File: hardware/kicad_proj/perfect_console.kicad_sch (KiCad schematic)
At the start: 71 parts, among them J1 R_Out, J10 PWR_OUT_Pins, J11 GPIO5-7, J12 USB_Out, J13 I2C, J14 ESP_UART, J15 GPIO41, J16 CH_UART, J17 CH_Flash, J18 Micro_SD_Card, J2 Jack_3.5, J3 L_Out, J4 USB, J5 TP4056_WO_Protect, J6 Bat, J7 PWR_Btn, J8 BTN_Pins, J9 PTT_Btn, Q1 NMOS, Q2 NMOS, Q3 NMOS, Q4 NMOS, Q5 NMOS, Q6 NMOS, SW1 Reset, SW2 Boot, U1 ESP32-S3-WROOM1, U2 Display, U3 PCM5102, U4 PAM8403, U5 CH32V006E8R6, U6 LoRa, U7 USBLC6-2SC6, U8 Mic, U9 DC-DC

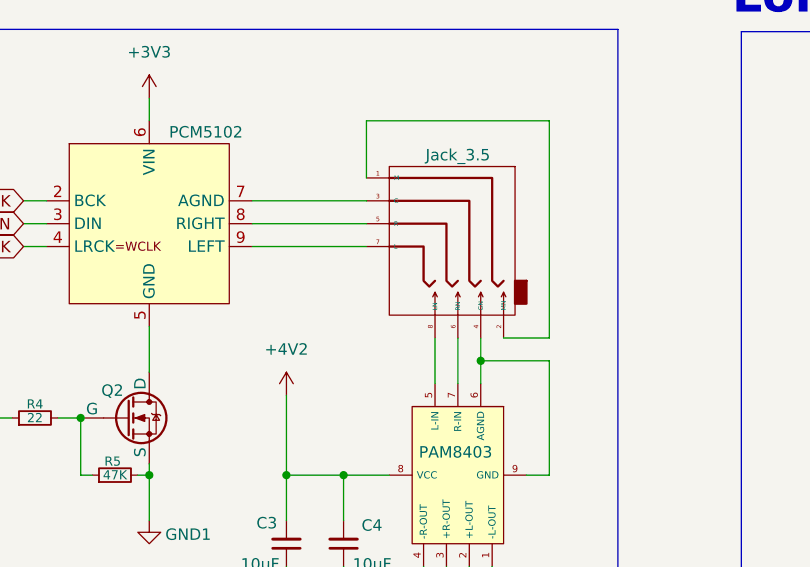
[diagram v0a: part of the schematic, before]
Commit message: Виправлено символ
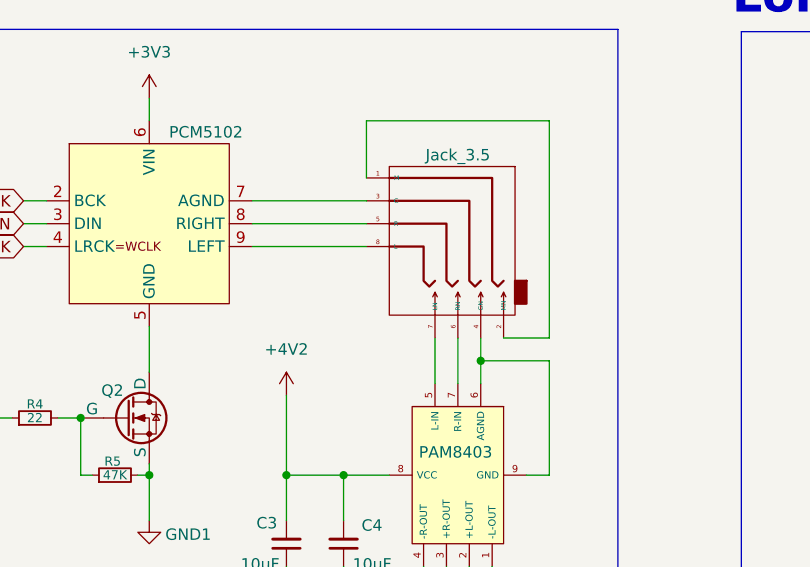
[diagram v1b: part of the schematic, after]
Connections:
- net at J2.7 (LN): now also U4.5 (L-IN); no longer U3.9 (LEFT)
- net at J2.8 (L): now also U3.9 (LEFT); no longer U4.5 (L-IN)

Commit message: Виправлено імена міток
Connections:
- net DISP_EN renamed DISP_PWR
- net LORA_EN renamed LORA_PWR
- net MIC_EN renamed MIC_PWR
- net POWER_EN renamed BOARD_PWR
- net SPK_EN renamed SPK_PWR
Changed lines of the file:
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@@
 		)
 	)
-	(global_label "DISP_EN"
+	(global_label "DISP_PWR"
 		(shape output)
 		(at 222.25 80.01 0)
@@
 		)
 		(property "Intersheetrefs" "${INTERSHEET_REFS}"
-			(at 233.0366 80.01 0)
+			(at 234.5485 80.01 0)
 			(effects
 				(font
@@
 		)
 	)
-	(global_label "SPK_EN"
+	(global_label "SPK_PWR"
 		(shape input)
 		(at 121.92 218.44 180)
@@
 		)
 		(property "Intersheetrefs" "${INTERSHEET_REFS}"
-			(at 111.7382 218.44 0)
-			(effects
-				(font
-					(size 1.27 1.27)
-				)
-				(justify right)
-				(hide yes)
-			)
-		)
-	)
-	(global_label "LORA_EN"
+			(at 110.2263 218.44 0)
+			(effects
+				(font
+					(size 1.27 1.27)
+				)
+				(justify right)
+				(hide yes)
+			)
+		)
+	)
+	(global_label "LORA_PWR"
 		(shape output)
 		(at 222.25 85.09 0)
@@
 		)
 		(property "Intersheetrefs" "${INTERSHEET_REFS}"
-			(at 233.3995 85.09 0)
+			(at 234.9114 85.09 0)
 			(effects
 				(font
@@
 		)
 	)
-	(global_label "LORA_EN"
+	(global_label "LORA_PWR"
 		(shape input)
 		(at 245.11 232.41 180)
@@
 		)
 		(property "Intersheetrefs" "${INTERSHEET_REFS}"
-			(at 233.9605 232.41 0)
+			(at 232.4486 232.41 0)
 			(effects
 				(font
@@
 		)
 	)
-	(global_label "MIC_EN"
+	(global_label "MIC_PWR"
 		(shape output)
 		(at 222.25 77.47 0)
@@
 		)
 		(property "Intersheetrefs" "${INTERSHEET_REFS}"
-			(at 232.0085 77.47 0)
+			(at 233.5204 77.47 0)
 			(effects
 				(font
@@
 		)
 	)
-	(global_label "SPK_EN"
+	(global_label "SPK_PWR"
 		(shape output)
 		(at 222.25 97.79 0)
@@
 		)
 		(property "Intersheetrefs" "${INTERSHEET_REFS}"
-			(at 232.4318 97.79 0)
+			(at 233.9437 97.79 0)
 			(effects
 				(font
@@
 		)
 	)
+	(global_label "BOARD_PWR"
+		(shape input)
+		(at 504.19 78.74 180)
+		(fields_autoplaced yes)
+		(effects
+			(font
+				(size 1.27 1.27)
+				(color 49 0 255 1)
+			)
+			(justify right)
+		)
+		(property "Intersheetrefs" "${INTERSHEET_REFS}"
+			(at 490.0167 78.74 0)
+			(effects
+				(font
+					(size 1.27 1.27)
+				)
+				(justify right)
+				(hide yes)
+			)
+		)
+	)
 	(global_label "LR_TX"
 		(shape output)
@@
 		)
 	)
-	(global_label "POWER_EN"
-		(shape input)
-		(at 504.19 78.74 180)
-		(fields_autoplaced yes)
-		(effects
-			(font
-				(size 1.27 1.27)
-				(color 255 139 0 1)
-			)
-			(justify right)
-		)
-		(property "Intersheetrefs" "${INTERSHEET_REFS}"
-			(at 491.2868 78.74 0)
-			(effects
-				(font
-					(size 1.27 1.27)
-				)
-				(justify right)
-				(hide yes)
-			)
-		)
-	)
 	(global_label "DATA -"
 		(shape bidirectional)
@@
 		)
 	)
-	(global_label "DISP_EN"
+	(global_label "DISP_PWR"
 		(shape input)
 		(at 49.53 224.79 180)
@@
 		)
 		(property "Intersheetrefs" "${INTERSHEET_REFS}"
-			(at 38.7434 224.79 0)
+			(at 37.2315 224.79 0)
 			(effects
 				(font
@@
 		)
 	)
-	(global_label "MIC_EN"
+	(global_label "MIC_PWR"
 		(shape input)
 		(at 354.33 207.01 180)
@@
 		)
 		(property "Intersheetrefs" "${INTERSHEET_REFS}"
-			(at 344.5715 207.01 0)
+			(at 343.0596 207.01 0)
 			(effects
 				(font
@@
 		)
 	)
-	(global_label "POWER_EN"
+	(global_label "BOARD_PWR"
 		(shape output)
 		(at 222.25 82.55 0)
@@
 		)
 		(property "Intersheetrefs" "${INTERSHEET_REFS}"
-			(at 235.1532 82.55 0)
-			(effects
-				(font
+			(at 236.4233 82.55 0)
+			(effects
+				(font

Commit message: Перепрацьовано схему
Карту пам'яті і дисплей рознесено на окремі шини
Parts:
- removed J11: GPIO5-7, Connector_PinHeader_2.54mm:PinHeader_1x03_P2.54mm_Vertical, symbol Connector_Generic:Conn_01x03
- added J11: GPIO_40-41, Connector_PinHeader_2.54mm:PinHeader_1x02_P2.54mm_Vertical, symbol Connector_Generic:Conn_01x02
- J15: value GPIO41 -> GPIO10
- renumbered C15 to C14, C16 to C15, U5 to U4, U4 to U5
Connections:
- net GPIO5 is gone; now on net LR_M0: U1.5 (IO5)
- net GPIO6 is gone; now on net LR_M1: U1.6 (IO6)
- net GPIO7 is gone; now on net LR_RX: U1.7 (IO7)
- net DISP_BLK: now also U1.12 (IO8); no longer U1.33 (IO40)
- net DISP_D/C: now also U1.11 (IO18); no longer U1.31 (IO38)
- net DISP_RST: now also U1.10 (IO17), U2.5 (RES); no longer U1.32 (IO39), U2.7 (CS)
- net GND1: now also J18.2 (DAT3/CD), U2.7 (CS)
- net GPIO41: now also J11.2 (Pin_2); no longer J15.1 (Pin_1)
- net LR_AUX: now also U1.9 (IO16); no longer U1.12 (IO8)
- net LR_M0: no longer U1.8 (IO15)
- net LR_M1: no longer U1.9 (IO16)
- net LR_RX: no longer U1.10 (IO17)
- net LR_TX: now also U1.8 (IO15); no longer U1.11 (IO18)
- net DISP_CS renamed SD_MOSI
- net SD_MOSI: now also J18.3 (CMD), R19.2; no longer U2.5 (RES)
- net HSPI_MISO renamed SD_MISO
- net SD_MISO: now also U1.32 (IO39); no longer U1.21 (IO13)
- removed net HSPI_MOSI: J18.3 (CMD), R19.2, U1.19 (IO11), U2.3 (SCL)
- net HSPI_SCK renamed SD_SCK
- net SD_SCK: now also U1.31 (IO38); no longer U1.20 (IO12), U2.4 (SDA)
- net SD_CS renamed GPIO10
- net GPIO10: now also J15.1 (Pin_1); no longer J18.2 (DAT3/CD)
- new net DISP_MISO: U1.21 (IO13)
- new net DISP_MOSI: U1.19 (IO11), U2.4 (SDA)
- new net DISP_SCK: U1.20 (IO12), U2.3 (SCL)
- new net GPIO40: J11.1 (Pin_1), U1.33 (IO40)
- no-connect marks 7 -> 8

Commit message: SD_CS пін перенесено на 10 пін ESP32S3
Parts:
- removed J15: GPIO10, Connector_PinHeader_2.54mm:PinHeader_1x01_P2.54mm_Vertical, symbol Connector_Generic:Conn_01x01
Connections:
- net GND1: no longer J18.2 (DAT3/CD)
- net GPIO10 renamed SD_CS
- net SD_CS: now also J18.2 (DAT3/CD)
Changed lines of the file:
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@@
 	(wire
 		(pts
-			(xy 511.81 215.9) (xy 514.35 215.9)
-		)
-		(stroke
-			(width 0)
-			(type default)
-		)
-	)
-	(wire
-		(pts
 			(xy 217.17 80.01) (xy 222.25 80.01)
 		)
@@
 		)
 	)
-	(global_label "GPIO10"
-		(shape bidirectional)
-		(at 511.81 215.9 180)
-		(fields_autoplaced yes)
-		(effects
-			(font
-				(size 1.27 1.27)
-				(color 1 34 255 1)
-			)
-			(justify right)
-		)
-		(property "Intersheetrefs" "${INTERSHEET_REFS}"
-			(at 500.8192 215.9 0)
-			(effects
-				(font
-					(size 1.27 1.27)
-				)
-				(justify right)
-				(hide yes)
-			)
-		)
-	)
 	(global_label "BACK_BTN"
 		(shape output)
@@
 		)
 	)
+	(global_label "SD_CS"
+		(shape output)
+		(at 46.99 88.9 180)
+		(fields_autoplaced yes)
+		(effects
+			(font
+				(size 1.27 1.27)
+				(color 255 0 37 1)
+			)
+			(justify right)
+		)
+		(property "Intersheetrefs" "${INTERSHEET_REFS}"
+			(at 38.0782 88.9 0)
+			(effects
+				(font
+					(size 1.27 1.27)
+				)
+				(justify right)
+				(hide yes)
+			)
+		)
+	)
 	(global_label "TX_0"
 		(shape output)
@@
 		)
 	)
-	(global_label "GPIO10"
-		(shape bidirectional)
-		(at 46.99 88.9 180)
-		(fields_autoplaced yes)
-		(effects
-			(font
-				(size 1.27 1.27)
-				(color 1 34 255 1)
-			)
-			(justify right)
-		)
-		(property "Intersheetrefs" "${INTERSHEET_REFS}"
-			(at 35.9992 88.9 0)
-			(effects
-				(font
-					(size 1.27 1.27)
-				)
-				(justify right)
-				(hide yes)
-			)
-		)
-	)
 	(global_label "SD_SCK"
 		(shape output)
@@
 		)
 	)
+	(global_label "SD_CS"
+		(shape input)
+		(at 591.82 40.64 180)
+		(fields_autoplaced yes)
+		(effects
+			(font
+				(size 1.27 1.27)
+				(color 255 0 37 1)
+			)
+			(justify right)
+		)
+		(property "Intersheetrefs" "${INTERSHEET_REFS}"
+			(at 582.9082 40.64 0)
+			(effects
+				(font
+					(size 1.27 1.27)
+				)
+				(justify right)
+				(hide yes)
+			)
+		)
+	)
 	(global_label "PTT_BTN"
 		(shape output)
@@
 	)
 	(symbol
-		(lib_id "Connector_Generic:Conn_01x01")
-		(at 519.43 215.9 0)
-		(unit 1)
-		(exclude_from_sim no)
-		(in_bom yes)
-		(on_board yes)
-		(dnp no)
-		(property "Reference" "J15"
-			(at 517.652 213.36 0)
-			(effects
-				(font
-					(size 1.27 1.27)
-				)
-				(justify left)
-				(hide yes)
-			)
-		)
-		(property "Value" "GPIO10"
-			(at 517.906 213.36 0)
-			(effects
-				(font
-					(size 1.27 1.27)
-				)
-				(justify left)
-			)
-		)
-		(property "Footprint" "Connector_PinHeader_2.54mm:PinHeader_1x01_P2.54mm_Vertical"
-			(at 519.43 215.9 0)
-			(effects
-				(font
-					(size 1.27 1.27)
-				)
-				(hide yes)
-			)
-		)
-		(property "Datasheet" "~"
-			(at 519.43 215.9 0)
-			(effects
-				(font
-					(size 1.27 1.27)
-				)
-				(hide yes)
-			)
-		)
-		(property "Description" "Generic connector, single row, 01x01, script generated (kicad-library-utils/schlib/autogen/connector/)"
-			(at 519.43 215.9 0)
-			(effects
-				(font
-					(size 1.27 1.27)
-				)
-				(hide yes)
-			)
-		)
-		(pin "1"
-		)
-		(instances
-			(project ""
-				(path "/17a56aab-f3dd-4de8-8a87-5e0772eddd26"
-					(reference "J15")
-					(unit 1)
-				)
-			)
-		)
-	)
-	(symbol
 		(lib_id "power:GND")
 		(at 420.37 228.6 270)
@@
 					(unit 1)
 				)
-			)
-		)
-	)
-	(symbol
-		(lib_id "power:GND")
-		(at 591.82 40.64 270)
-		(mirror x)
-		(unit 1)
-		(exclude_from_sim no)
-		(in_bom yes)
-		(on_board yes)
-		(dnp no)
-		(fields_autoplaced yes)
-		(property "Reference" "#PWR54"
-			(at 585.47 40.64 0)
-			(effects
-				(font
-					(size 1.27 1.27)
-				)
-				(hide yes)
-			)
-		)
-		(property "Value" "GND1"
-			(at 588.01 40.6399 90)
-			(effects
-				(font
-					(size 1.27 1.27)
-				)
-				(justify right)
-			)
-		)
-		(property "Footprint" ""
-			(at 591.82 40.64 0)
-			(effects
-				(font
-					(size 1.27 1.27)
-				)
-				(hide yes)
-			)
-		)
-		(property "Datasheet" ""
-			(at 591.82 40.64 0)
-			(effects
-				(font
-					(size 1.27 1.27)
-				)
-				(hide yes)
-			)
-		)
-		(property "Description" "Power symbol creates a global label with name \"GND\" , ground"
-			(at 591.82 40.64 0)
-			(effects
-				(font
-					(size 1.27 1.27)
-				)
-				(hide yes)
-			)
-		)
-		(pin "1"
-		)
-		(instances
-			(project "perfect_console"
-				(path "/17a56aab-f3dd-4de8-8a87-5e0772eddd26"
-					(reference "#PWR54")
-					(unit 1)
-				)

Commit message: Додано фільтруючий конденсатор на VVAL
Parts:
- added C12: 100nF, Capacitor_SMD:C_1206_3216Metric, symbol Device:C_Small
- renumbered C12 to C13, C13 to C14, C14 to C15, C15 to C16, J16 to J15, J17 to J16, J18 to J17
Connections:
- net GND1: now also C12.1
- net VVAL: now also C12.2
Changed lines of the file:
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@@
 	)
 	(junction
+		(at 433.07 77.47)
+		(diameter 0)
+		(color 0 0 0 0)
+	)
+	(junction
 		(at 66.04 48.26)
 		(diameter 0)
@@
 	(wire
 		(pts
+			(xy 427.99 69.85) (xy 427.99 67.31)
+		)
+		(stroke
+			(width 0)
+			(type default)
+		)
+	)
+	(wire
+		(pts
 			(xy 81.28 86.36) (xy 85.09 86.36)
 		)
@@
 	(wire
 		(pts
+			(xy 427.99 77.47) (xy 433.07 77.47)
+		)
+		(stroke
+			(width 0)
+			(type default)
+		)
+	)
+	(wire
+		(pts
 			(xy 610.87 92.71) (xy 610.87 99.06)
 		)
@@
 	(wire
 		(pts
+			(xy 427.99 74.93) (xy 427.99 77.47)
+		)
+		(stroke
+			(width 0)
+			(type default)
+		)
+	)
+	(wire
+		(pts
 			(xy 568.96 228.6) (xy 572.77 228.6)
 		)
@@
 	(wire
 		(pts
-			(xy 471.17 72.39) (xy 471.17 80.01)
+			(xy 471.17 72.39) (xy 471.17 81.28)
 		)
 		(stroke
@@
 	(wire
 		(pts
+			(xy 433.07 77.47) (xy 433.07 81.28)
+		)
+		(stroke
+			(width 0)
+			(type default)
+		)
+	)
+	(wire
+		(pts
 			(xy 46.99 78.74) (xy 50.8 78.74)
 		)
@@
 	(wire
 		(pts
-			(xy 379.73 59.69) (xy 379.73 66.04)
+			(xy 379.73 59.69) (xy 379.73 69.85)
 		)
 		(stroke
@@
 	(wire
 		(pts
+			(xy 427.99 67.31) (xy 433.07 67.31)
+		)
+		(stroke
+			(width 0)
+			(type default)
+		)
+	)
+	(wire
+		(pts
 			(xy 554.99 205.74) (xy 565.15 205.74)
 		)
@@
 	(wire
 		(pts
-			(xy 400.05 66.04) (xy 400.05 71.12)
+			(xy 400.05 66.04) (xy 400.05 69.85)
 		)
 		(stroke
@@
 	(symbol
 		(lib_id "power:GND")
-		(at 400.05 71.12 0)
+		(at 400.05 69.85 0)
 		(mirror y)
 		(unit 1)
@@
 		(dnp no)
 		(property "Reference" "#PWR33"
-			(at 400.05 77.47 0)
+			(at 400.05 76.2 0)
 			(effects
 				(font
@@
 		)
 		(property "Footprint" ""
-			(at 400.05 71.12 0)
+			(at 400.05 69.85 0)
 			(effects
 				(font
@@
 		)
 		(property "Datasheet" ""
-			(at 400.05 71.12 0)
+			(at 400.05 69.85 0)
 			(effects
 				(font
@@
 		)
 		(property "Description" "Power symbol creates a global label with name \"GND\" , ground"
-			(at 400.05 71.12 0)
+			(at 400.05 69.85 0)
 			(effects
 				(font
@@
 		(on_board yes)
 		(dnp no)
-		(property "Reference" "#PWR56"
+		(property "Reference" "#PWR55"
 			(at 632.46 88.9 0)
 			(effects
@@
 			(project "perfect_console"
 				(path "/17a56aab-f3dd-4de8-8a87-5e0772eddd26"
-					(reference "#PWR56")
+					(reference "#PWR55")
 					(unit 1)
 				)
@@
 		(on_board yes)
 		(dnp no)
-		(property "Reference" "J17"
+		(property "Reference" "J16"
 			(at 624.332 191.262 0)
 			(effects
@@
 			(project "perfect_console"
 				(path "/17a56aab-f3dd-4de8-8a87-5e0772eddd26"
-					(reference "J17")
+					(reference "J16")
 					(unit 1)
 				)
@@
 		(on_board yes)
 		(dnp no)
-		(property "Reference" "C15"
+		(property "Reference" "C16"
 			(at 635.254 93.98 90)
 			(effects
@@
 			(project "perfect_console"
 				(path "/17a56aab-f3dd-4de8-8a87-5e0772eddd26"
-					(reference "C15")
+					(reference "C16")
 					(unit 1)
 				)
@@
 		(on_board yes)
 		(dnp no)
-		(property "Reference" "#PWR55"
+		(property "Reference" "#PWR54"
 			(at 610.87 96.52 0)
 			(effects
@@
 			(project "perfect_console"
 				(path "/17a56aab-f3dd-4de8-8a87-5e0772eddd26"
-					(reference "#PWR55")
+					(reference "#PWR54")
 					(unit 1)
 				)
@@
 	(symbol
 		(lib_id "power:GND")
-		(at 379.73 66.04 0)
+		(at 379.73 69.85 0)
 		(mirror y)
 		(unit 1)
@@
 		(fields_autoplaced yes)
 		(property "Reference" "#PWR32"
-			(at 379.73 72.39 0)
+			(at 379.73 76.2 0)
 			(effects
 				(font
@@
 		)
 		(property "Value" "GND"
-			(at 379.73 71.12 0)
+			(at 379.73 74.93 0)
 			(effects
 				(font
@@
 		)
 		(property "Footprint" ""
-			(at 379.73 66.04 0)
+			(at 379.73 69.85 0)
 			(effects
 				(font
@@
 		)
 		(property "Datasheet" ""
-			(at 379.73 66.04 0)
+			(at 379.73 69.85 0)
 			(effects
 				(font
@@
 		)
 		(property "Description" "Power symbol creates a global label with name \"GND\" , ground"
-			(at 379.73 66.04 0)
+			(at 379.73 69.85 0)
 			(effects
 				(font
@@
 	(symbol
 		(lib_id "power:GND")
-		(at 471.17 80.01 0)
+		(at 471.17 81.28 0)
 		(mirror y)
 		(unit 1)
@@
 		(fields_autoplaced yes)
 		(property "Reference" "#PWR40"
-			(at 471.17 86.36 0)
+			(at 471.17 87.63 0)
 			(effects
 				(font
@@
 		)
 		(property "Value" "GND1"
-			(at 471.17 85.09 0)
+			(at 471.17 86.36 0)
 			(effects
 				(font
@@
 		)
 		(property "Footprint" ""
-			(at 471.17 80.01 0)
+			(at 471.17 81.28 0)
 			(effects
 				(font
@@
 		)
 		(property "Datasheet" ""
-			(at 471.17 80.01 0)
+			(at 471.17 81.28 0)
 			(effects
 				(font
@@
 		)
 		(property "Description" "Power symbol creates a global label with name \"GND\" , ground"
-			(at 471.17 80.01 0)
+			(at 471.17 81.28 0)
 			(effects
 				(font
@@
 		(dnp no)
 		(fields_autoplaced yes)
-		(property "Reference" "#PWR57"
+		(property "Reference" "#PWR56"
 			(at 650.24 106.68 0)
 			(effects
@@
 			(project "perfect_console"
 				(path "/17a56aab-f3dd-4de8-8a87-5e0772eddd26"
-					(reference "#PWR57")
+					(reference "#PWR56")
 					(unit 1)
 				)
@@
 		(on_board yes)
 		(dnp no)
-		(property "Reference" "C14"
+		(property "Reference" "C15"
 			(at 639.318 86.36 90)
 			(effects
@@
 			(project "perfect_console"
 				(path "/17a56aab-f3dd-4de8-8a87-5e0772eddd26"
-					(reference "C14")
+					(reference "C15")
 					(unit 1)
 				)
@@
 		(on_board yes)
 		(dnp no)
-		(property "Reference" "J18"
+		(property "Reference" "J17"
 			(at 635.508 54.102 0)
 			(effects
@@
 			(project "perfect_console"
 				(path "/17a56aab-f3dd-4de8-8a87-5e0772eddd26"
-					(reference "J18")
+					(reference "J17")
 					(unit 1)
 				)
@@
 	(symbol
 		(lib_id "Device:C_Small")
-		(at 471.17 64.77 0)
+		(at 427.99 72.39 180)
 		(unit 1)
 		(exclude_from_sim no)
@@
 		(dnp no)
 		(property "Reference" "C12"
+			(at 424.942 69.85 0)
+			(effects
+				(font
+					(size 1.27 1.27)
+				)
+				(justify left)
+			)
+		)
+		(property "Value" "100nF"
+			(at 426.466 75.184 0)
+			(effects
+				(font
+					(size 1.27 1.27)
+				)
+				(justify left)
+			)
+		)
+		(property "Footprint" "Capacitor_SMD:C_1206_3216Metric"
+			(at 427.99 72.39 0)
+			(effects
+				(font
+					(size 1.27 1.27)
+				)
+				(hide yes)
+			)
+		)
+		(property "Datasheet" "~"
+			(at 427.99 72.39 0)
+			(effects
+				(font
+					(size 1.27 1.27)
+				)
+				(hide yes)
+			)
+		)
+		(property "Description" "Unpolarized capacitor, small symbol"
+			(at 427.99 72.39 0)
+			(effects
+				(font
+					(size 1.27 1.27)
+				)
+				(hide yes)
+			)
+		)
+		(pin "1"
+		)
+		(pin "2"
+		)
+		(instances
+			(project "perfect_console"
+				(path "/17a56aab-f3dd-4de8-8a87-5e0772eddd26"
+					(reference "C12")
+					(unit 1)
+				)
+			)
+		)
+	)
+	(symbol
+		(lib_id "Device:C_Small")
+		(at 471.17 64.77 0)
+		(unit 1)
+		(exclude_from_sim no)
+		(in_bom yes)
+		(on_board yes)
+		(dnp no)
+		(property "Reference" "C13"
 			(at 465.836 63.246 0)
 			(effects
@@
 			(project "perfect_console"
 				(path "/17a56aab-f3dd-4de8-8a87-5e0772eddd26"
-					(reference "C12")
+					(reference "C13")
 					(unit 1)
 				)
@@
 		(on_board yes)
 		(dnp no)
-		(property "Reference" "C13"
+		(property "Reference" "C14"
 			(at 559.816 197.866 0)
 			(effects
@@
 			(project "perfect_console"
 				(path "/17a56aab-f3dd-4de8-8a87-5e0772eddd26"
-					(reference "C13")
+					(reference "C14")
 					(unit 1)
 				)
@@
 	(symbol
 		(lib_id "power:GND")
-		(at 433.07 77.47 0)
+		(at 433.07 81.28 0)
 		(mirror y)
 		(unit 1)
@@
 		(fields_autoplaced yes)
 		(property "Reference" "#PWR38"
-			(at 433.07 83.82 0)
+			(at 433.07 87.63 0)
 			(effects
 				(font
@@
 		)
 		(property "Value" "GND1"
-			(at 433.07 82.55 0)
+			(at 433.07 86.36 0)
 			(effects
 				(font
@@
 		)
 		(property "Footprint" ""
-			(at 433.07 77.47 0)
+			(at 433.07 81.28 0)
 			(effects
 				(font
@@
 		)
 		(property "Datasheet" ""
-			(at 433.07 77.47 0)
+			(at 433.07 81.28 0)
 			(effects
 				(font
@@
 		)
 		(property "Description" "Power symbol creates a global label with name \"GND\" , ground"
-			(at 433.07 77.47 0)
+			(at 433.07 81.28 0)
 			(effects
 				(font
@@
 		(on_board yes)
 		(dnp no)
-		(property "Reference" "J16"
+		(property "Reference" "J15"
 			(at 621.792 220.726 0)
 			(effects
@@
 			(project "perfect_console"
 				(path "/17a56aab-f3dd-4de8-8a87-5e0772eddd26"
-					(reference "J16")
+					(reference "J15")
 					(unit 1)
 				)
